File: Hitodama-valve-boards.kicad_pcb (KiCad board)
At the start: 2 copper layers, 66 x 64.8 mm, 35 parts, among them J1 Solenoid A, J10 PWMB, J11 STANDBY, J12 +12v_SUPPLY, J13 VCC supply, J14 GND, J2 Solenoid B, J3 Pressure_amp_b, J4 Pressure_amp_a, J5 PWMA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

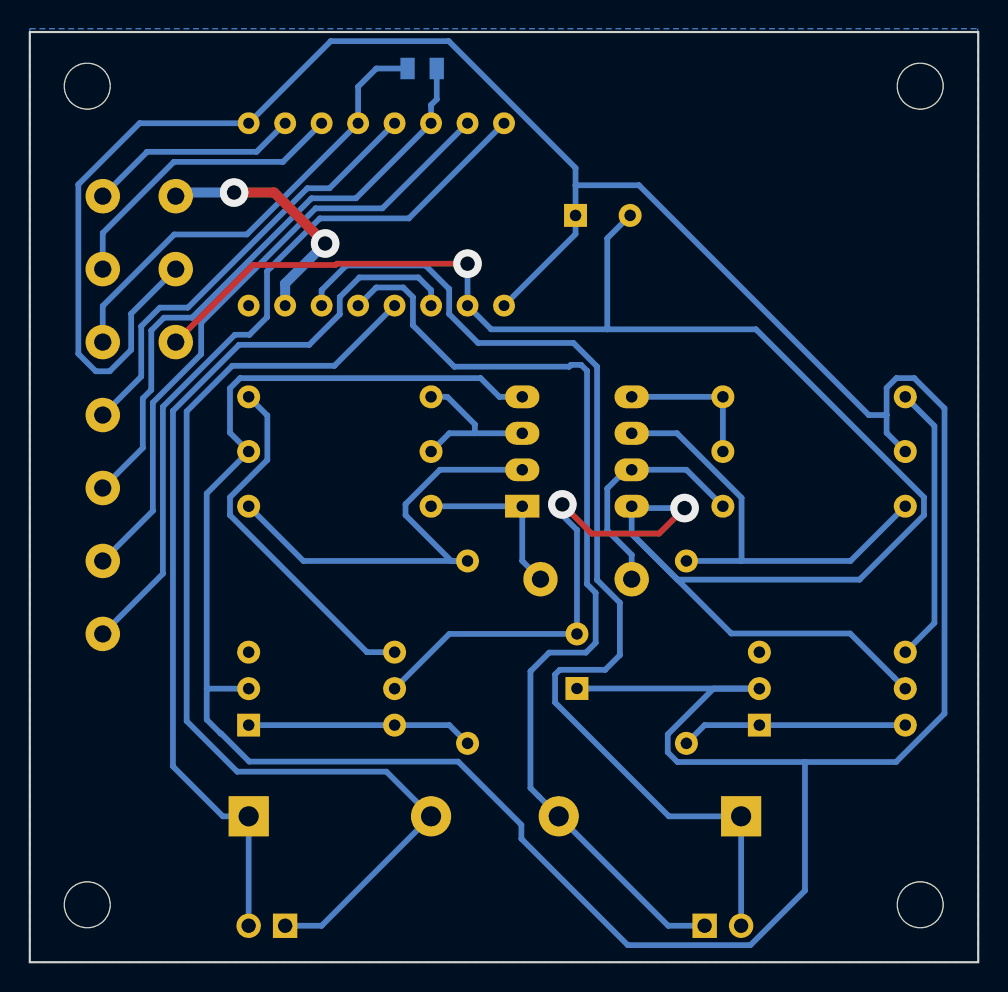
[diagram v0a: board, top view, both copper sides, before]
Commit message: Separate the two board into different sch files. Added missing jumper (SCH only) and missing Vias for a jumber
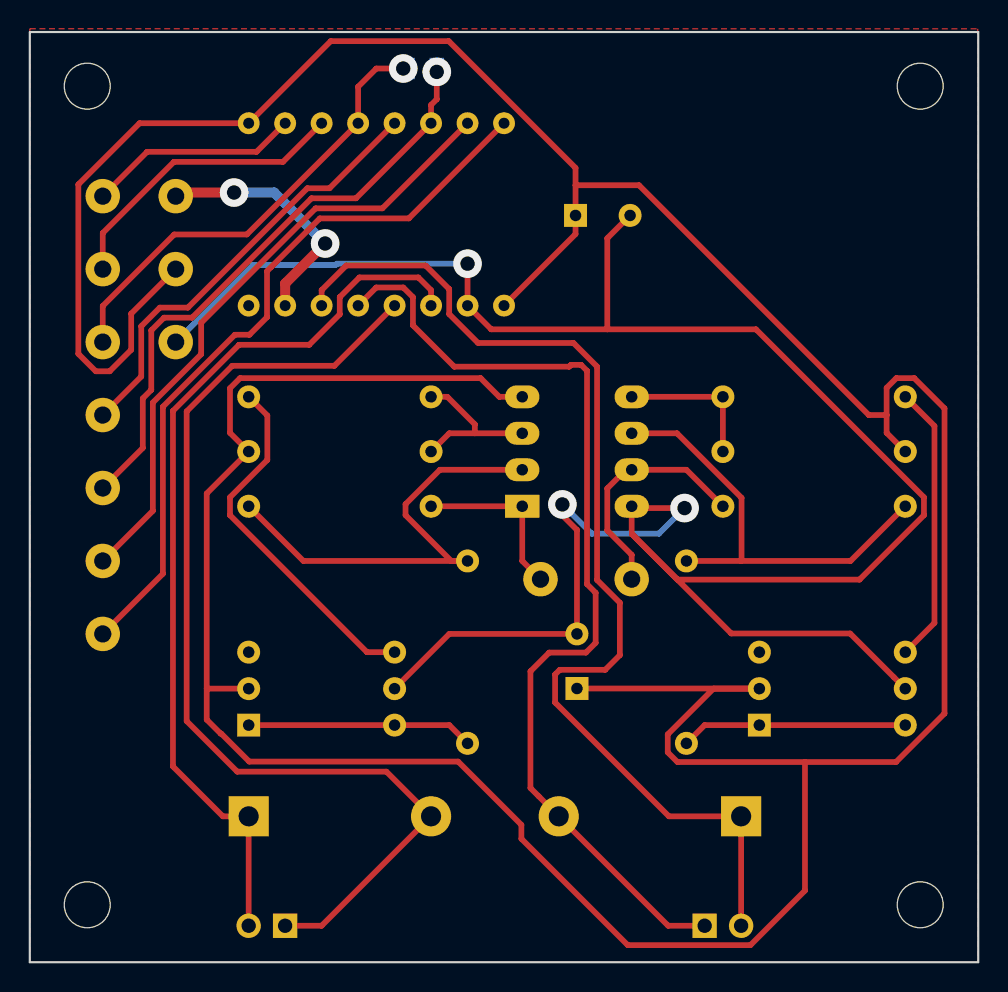
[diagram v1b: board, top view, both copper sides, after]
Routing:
- net Net-(J8-Pad1): vias 0 -> 1
- net Net-(J7-Pad1): vias 0 -> 1
- added copper zone on F.Cu, net GND
- removed copper zone on B.Cu, net GND

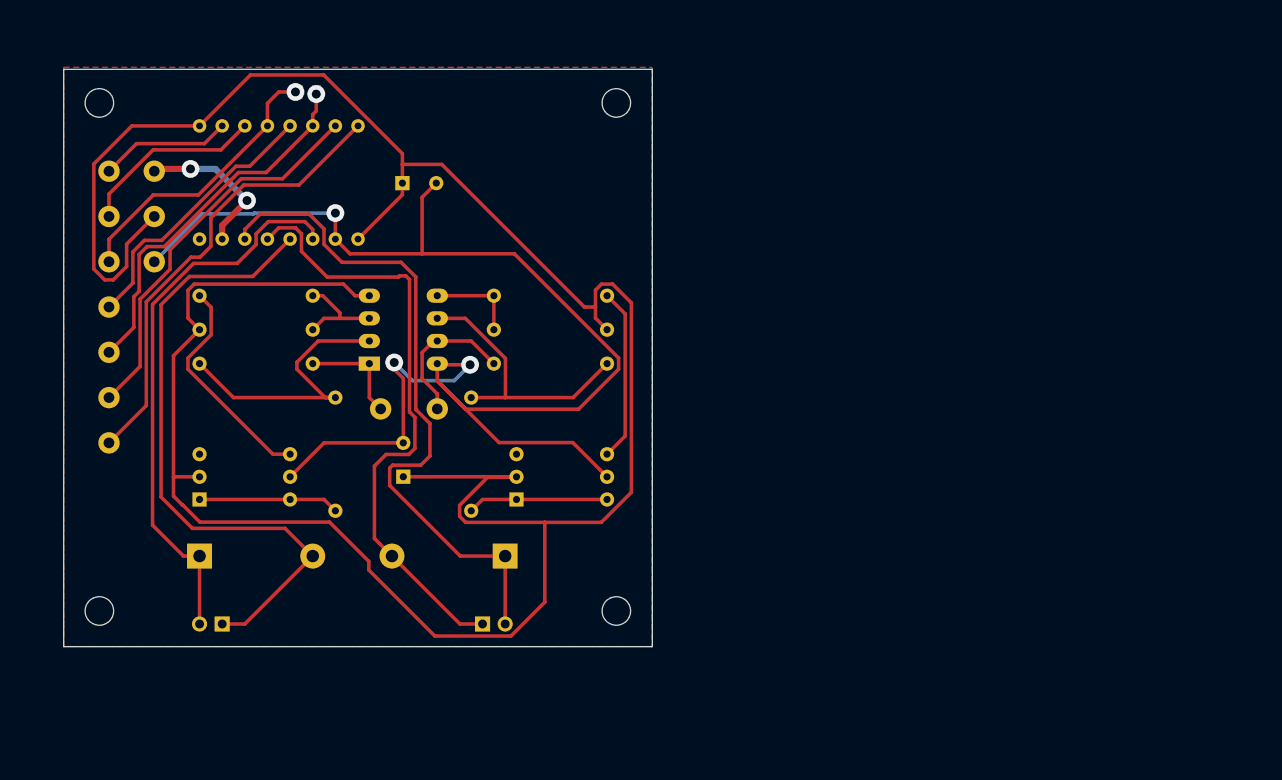
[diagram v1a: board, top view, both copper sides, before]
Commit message: Coordinate Connectors on both boards
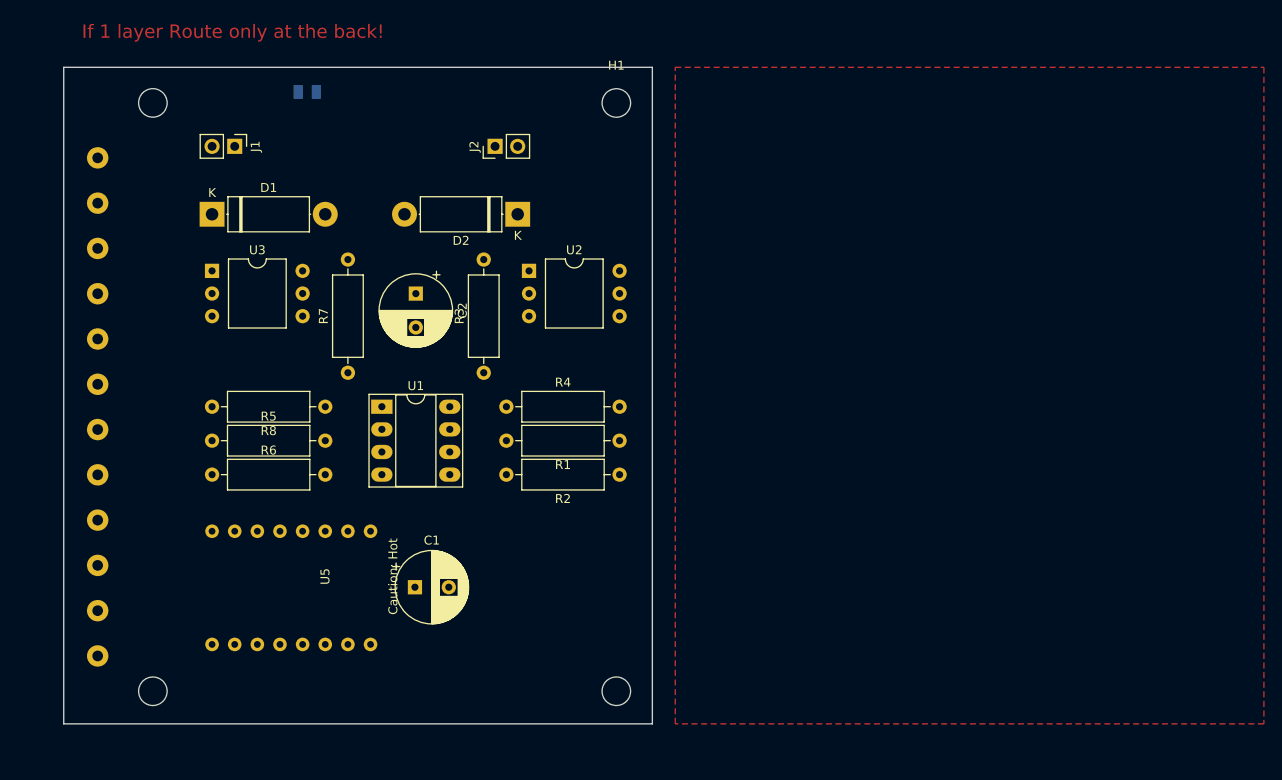
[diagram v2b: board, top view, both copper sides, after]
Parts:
- C1, C2, D1, D2, H1, J1, J2, R1, R2, R3, R4, R5, R6, R7, R8, U1, U2, U3, U5: moved to F.Cu
- moved J1 53.6 mm to (19.2, 8.87), turned to 270 degrees
- moved J2 53.6 mm to (48.4, 8.87), turned to 90 degrees
- moved C1 45.4 mm to (39.4, 58.3)
- moved J3 44.3 mm to (3.81, 61.0), turned to 90 degrees
- moved J11 39.2 mm to (3.81, 66.0)
- moved D1 38.4 mm to (16.6, 16.5)
- moved D2 38.4 mm to (50.9, 16.5)
- moved J4 36.3 mm to (3.81, 55.9)
- moved U5 32.8 mm to (34.4, 52.0), turned to 270 degrees
- moved J5 32.0 mm to (3.81, 10.2)
- moved J12 29.7 mm to (3.81, 40.6), turned to 0 degrees
- moved J14 29.7 mm to (3.81, 45.7), turned to 90 degrees
- moved J13 29.7 mm to (3.81, 50.8), turned to 90 degrees
- moved U2 25.7 mm to (52.2, 22.8)
- moved U3 25.7 mm to (16.6, 22.8)
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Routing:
- net GND: track 288.0 -> 0.00 mm
- net VCC: track 159.2 -> 0.00 mm, vias 3 -> 0
- net Net-(D2-Pad1): track 76.5 -> 0.00 mm
- net Net-(D1-Pad2): track 72.2 -> 0.00 mm
- net Net-(D2-Pad2): track 68.9 -> 0.00 mm
- net Net-(D1-Pad1): track 63.1 -> 0.00 mm
- net Net-(J5-Pad1): track 51.4 -> 0.00 mm
- net Net-(J6-Pad1): track 43.7 -> 0.00 mm
- net Net-(J7-Pad1): track 41.8 -> 0.00 mm, vias 1 -> 0
- net Net-(R7-Pad1): track 32.3 -> 0.00 mm
- net Net-(J8-Pad1): track 32.1 -> 0.00 mm, vias 1 -> 0
- net /stby: track 30.8 -> 0.00 mm
- net Net-(R3-Pad1): track 30.7 -> 0.00 mm
- net Net-(R6-Pad1): track 25.3 -> 0.00 mm
- net Net-(J9-Pad1): track 20.9 -> 0.00 mm
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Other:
- board size 66 x 64.8 mm -> 66 x 73.7 mm
- net class Default: clearance 0.3 -> 0.31; trace_width 0.4 -> 0.31
- net class powers removed
- rule trace_clearance: 0.3 -> 0.31
- board text added: "If 1 layer Route only at the back!"

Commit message: (auto) routing
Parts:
- removed J10: PWMB, Connector_Pin:Pin_D1.0mm_L10.0mm_LooseFit
- removed J11: STANDBY, Connector_Pin:Pin_D1.0mm_L10.0mm_LooseFit
- removed J12: +12v_SUPPLY, Connector_Pin:Pin_D1.0mm_L10.0mm_LooseFit
- removed J13: VCC supply, Connector_Pin:Pin_D1.0mm_L10.0mm_LooseFit
- removed J14: GND, Connector_Pin:Pin_D1.0mm_L10.0mm_LooseFit
- removed J3: Pressure_amp_b, Connector_Pin:Pin_D1.0mm_L10.0mm_LooseFit
- removed J4: Pressure_amp_a, Connector_Pin:Pin_D1.0mm_L10.0mm_LooseFit
- removed J5: PWMA, Connector_Pin:Pin_D1.0mm_L10.0mm_LooseFit
- removed J6: AIN2, Connector_Pin:Pin_D1.0mm_L10.0mm_LooseFit
- removed J7: AIN1, Connector_Pin:Pin_D1.0mm_L10.0mm_LooseFit
- removed J8: BIN1, Connector_Pin:Pin_D1.0mm_L10.0mm_LooseFit
- removed J9: BIN2, Connector_Pin:Pin_D1.0mm_L10.0mm_LooseFit
- added JP2: (A,B)IN 1, Jumper:SolderJumper-2_P1.3mm_Bridged2Bar_Pad1.0x1.5mm, B.Cu at (6.35, 11.4)
- added U4: ChamberBoard_Holder, chamber_board_holder:chamber_board_holder, F.Cu at (2.54, 8.89)
- J1, J2: footprint Connector_PinHeader_2.54mm:PinHeader_1x02_P2.54mm_Vertical -> TerminalBlock:TerminalBlock_Altech_AK300-2_P5.00mm
- moved JP1 32.8 mm to (6.35, 27.9), turned to 270 degrees
- moved J1 5.95 mm to (25.0, 7.62), turned to 180 degrees
- moved J2 2.95 mm to (45.7, 7.62), turned to 180 degrees
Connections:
- net Net-(D1-Pad1) renamed /HVA+
- net Net-(D1-Pad2) renamed /HVA-
- net Net-(D2-Pad1) renamed /HVB+
- net Net-(D2-Pad2) renamed /HVB-
- net Net-(J3-Pad1) renamed /B.PRESSURE
- net Net-(J4-Pad1) renamed /A.PRESSURE
- net Net-(J7-Pad1) renamed /A.IN.1
- net Net-(J8-Pad1) renamed /B.IN.1
- U5 pad 10: Net-(J10-Pad1) -> /B.PWM
- U5 pad 11: Net-(J9-Pad1) -> /B.IN.2
- U5 pad 15: Net-(J6-Pad1) -> /A.IN.2
- U5 pad 16: Net-(J5-Pad1) -> /A.PWM
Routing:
- net GND: track 0.00 -> 242.7 mm
- net VCC: track 0.00 -> 177.6 mm
- net /HVB+: track 0.00 -> 112.3 mm
- net /A.PRESSURE: track 0.00 -> 89.5 mm
- net /B.PWM: track 0.00 -> 82.3 mm
- net /HVA-: track 0.00 -> 80.7 mm
- net /B.PRESSURE: track 0.00 -> 79.5 mm
- net /A.PWM: track 0.00 -> 75.2 mm
- net +12V: track 0.00 -> 74.4 mm
- net /A.IN.1: track 0.00 -> 61.7 mm
- net /HVB-: track 0.00 -> 61.1 mm, vias 0 -> 2
- net /HVA+: track 0.00 -> 60.2 mm
- net /A.IN.2: track 0.00 -> 57.6 mm, vias 0 -> 2
- net /B.IN.1: track 0.00 -> 48.5 mm
- net /B.IN.2: track 0.00 -> 38.4 mm
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- added copper zone on B.Cu, net GND
- removed copper zone on F.Cu, net GND

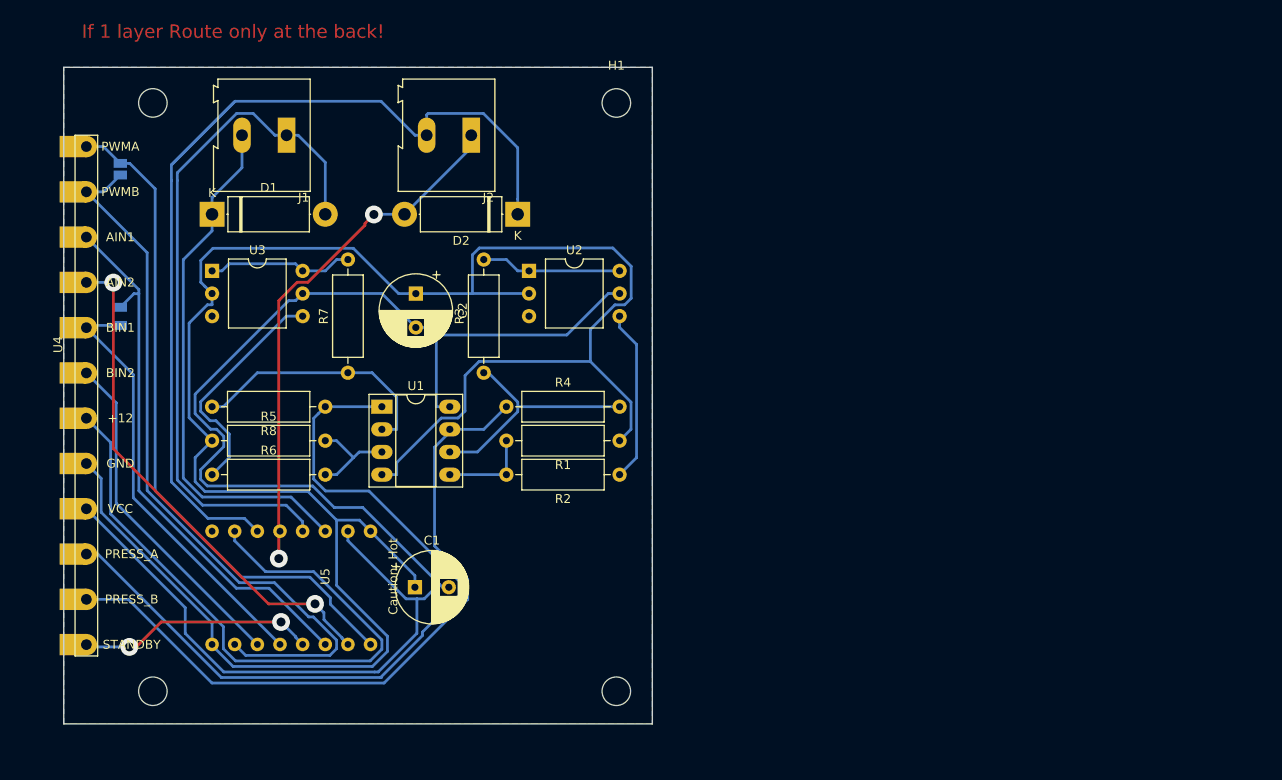
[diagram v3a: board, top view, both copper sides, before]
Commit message: separated the teensy board into four modules, so that it fits in smaller PCB's. Improved the chamber board, and added rules so that auto-router can figure out the optimal 1 layer+jumpers route
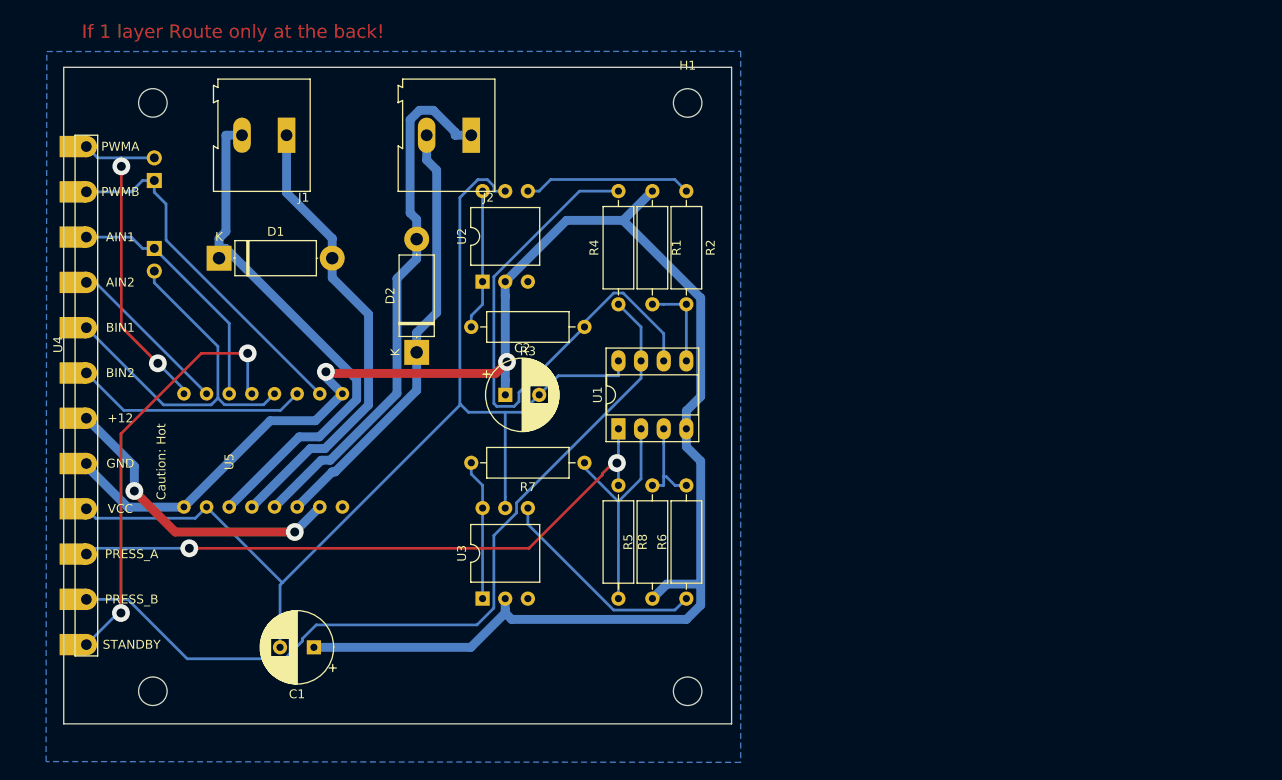
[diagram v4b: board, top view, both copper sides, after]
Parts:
- JP1, JP2: footprint Jumper:SolderJumper-2_P1.3mm_Bridged2Bar_Pad1.0x1.5mm -> Connector_PinHeader_2.54mm:PinHeader_1x02_P2.54mm_Vertical
- moved R6 55.0 mm to (69.9, 59.6), turned to 90 degrees
- moved R5 52.5 mm to (66.0, 59.6), turned to 90 degrees
- moved U3 47.7 mm to (47.0, 59.6), turned to 90 degrees
- moved R8 34.1 mm to (62.2, 46.9), turned to 270 degrees
- moved R2 32.7 mm to (69.9, 13.9), turned to 270 degrees
- moved R7 28.4 mm to (58.4, 44.4), turned to 180 degrees
- moved R1 28.2 mm to (66.0, 13.9), turned to 270 degrees
- moved U1 26.7 mm to (62.2, 40.6), turned to 90 degrees
- moved U5 21.1 mm to (13.5, 49.3), turned to 90 degrees
- moved D2 19.2 mm to (39.6, 32.0), turned to 90 degrees
- moved R4 17.0 mm to (62.2, 26.6), turned to 90 degrees
- moved C2 15.2 mm to (49.5, 36.7), turned to 0 degrees
- moved C1 13.2 mm to (28.1, 65.1), turned to 180 degrees
- moved R3 12.4 mm to (58.4, 29.1), turned to 180 degrees
- moved JP1 8.52 mm to (10.2, 20.3), turned to 180 degrees
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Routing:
- net /HVB+: track 112.3 -> 48.8 mm
- net VCC: track 177.6 -> 124.3 mm
- net GND: track 242.7 -> 195.7 mm, vias 0 -> 2
- net /B.PWM: track 82.3 -> 39.8 mm
- net +12V: track 74.4 -> 34.3 mm, vias 0 -> 2
- net /A.IN.2: track 57.6 -> 18.7 mm, vias 2 -> 0
- net /A.PWM: track 75.2 -> 37.5 mm, vias 0 -> 2
- net Net-(R3-Pad1): track 27.2 -> 62.5 mm
- net /A.IN.1: track 61.7 -> 27.9 mm
- net /HVA-: track 80.7 -> 51.9 mm
- net /stby: track 26.6 -> 48.1 mm
- net /A.PRESSURE: track 89.5 -> 70.4 mm, vias 0 -> 2
- net /B.PRESSURE: track 79.5 -> 93.0 mm
- net /B.IN.2: track 38.4 -> 26.2 mm
- net /B.IN.1: track 48.5 -> 43.0 mm
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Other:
- board size 66 x 73.7 mm -> 74.9 x 73.7 mm
- net class Power added: clearance 0.31, trace_width 1, via_dia 2, via_drill 1

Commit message: even greater trace widths
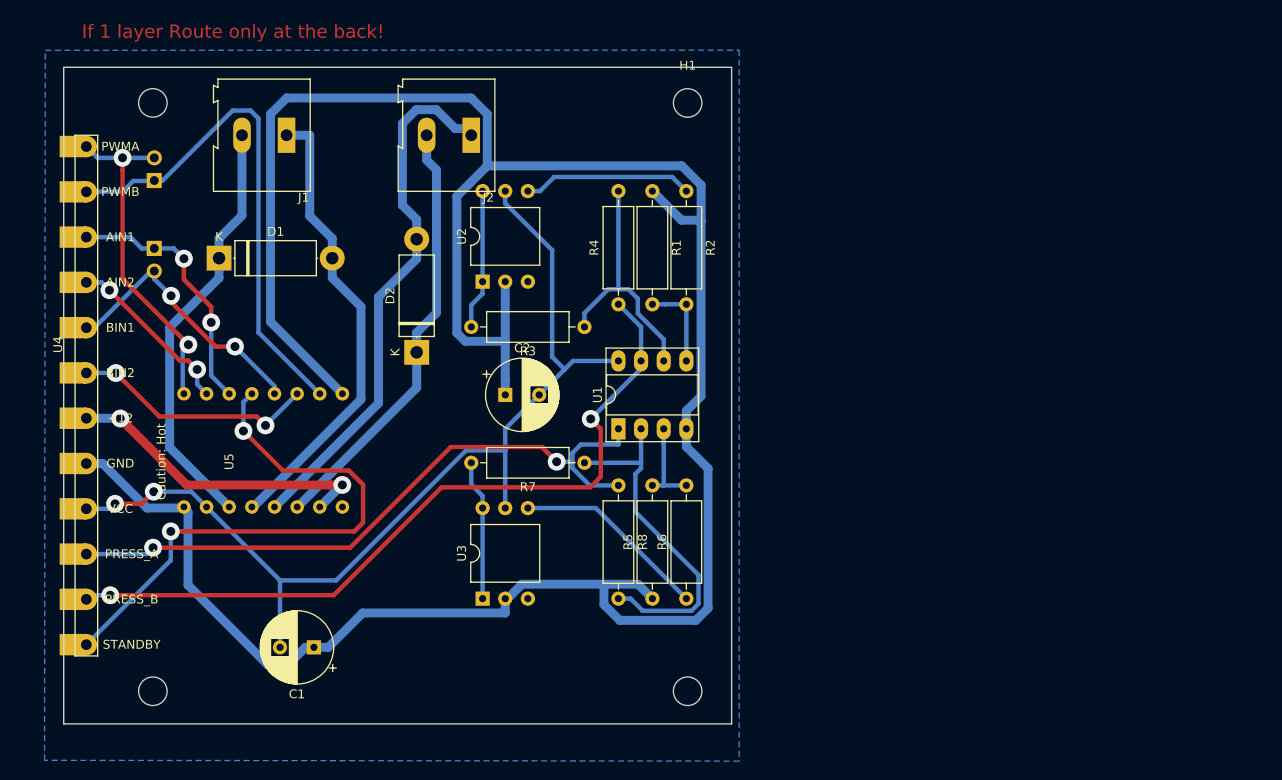
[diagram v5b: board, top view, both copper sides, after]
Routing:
- net GND: track 195.7 -> 284.8 mm, vias 2 -> 0
- net Net-(R3-Pad1): track 62.5 -> 29.0 mm
- net /B.PWM: track 39.8 -> 57.2 mm
- net /stby: track 48.1 -> 63.3 mm
- net Net-(R7-Pad1): track 26.0 -> 39.1 mm
- net /B.IN.1: track 43.0 -> 30.9 mm, vias 0 -> 2
- net VCC: track 124.3 -> 113.0 mm, vias 0 -> 2
- net /HVA+: track 59.0 -> 47.8 mm
- net /B.PRESSURE: track 93.0 -> 86.6 mm, vias 0 -> 2
- net /A.PRESSURE: track 70.4 -> 75.2 mm
- net Net-(R6-Pad1): track 24.1 -> 22.0 mm
- net /B.IN.2: track 26.2 -> 27.6 mm, vias 0 -> 2
- net /A.IN.1: track 27.9 -> 29.2 mm, vias 0 -> 2
- net +12V: track 34.3 -> 35.4 mm
- net /A.IN.2: track 18.7 -> 19.6 mm, vias 0 -> 2
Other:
- net class Default: trace_width 0.31 -> 0.5
